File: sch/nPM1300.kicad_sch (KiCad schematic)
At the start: 24 parts, among them J1 USB_C_Receptacle_USB2.0_16P, J4 Conn_01x02_MountingPin, U2 nPM1300-QEAA, U5 USBLC6-2P6

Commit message: Updates for rev 1
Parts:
- added D2: LED_Red, LED_SMD:LED_0603_1608Metric, symbol Device:LED_Small
- added D3: LED_Green, LED_SMD:LED_0603_1608Metric, symbol Device:LED_Small
- added D4: LED_Blue, LED_SMD:LED_0603_1608Metric, symbol Device:LED_Small
- added TP10, TP11, TP12, TP13, TP3, TP4, TP5, TP6, TP7, TP8, TP9: TestPoint, TestPoint:TestPoint_Pad_D1.0mm, symbol Connector:TestPoint
- C14, C21: LCSC (none) -> C15849
- C15: LCSC (none) -> C467016
- C16, C17, C18, C19, C22, C23, C24, C25, C26: LCSC (none) -> C19702
- C20: LCSC (none) -> C23630
- F1: LCSC (none) -> C516069
- J1: LCSC (none) -> C165948
- J4: LCSC (none) -> C5118738
- L5, L6: LCSC (none) -> C412023
- R2: LCSC (none) -> C138139
- R3: LCSC (none) -> C274343
- R6, R7: LCSC (none) -> C270344
- U2: LCSC (none) -> C7466043
- U5: LCSC (none) -> C15999
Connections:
- net NTC is gone; now on net GND: U2.18 (NTC)
- net LSOUT1: now also TP9.1
- net LSOUT2: now also TP10.1
- net SCL: now also TP12.1
- net SDA: now also TP11.1
- net VBUSIN: now also TP4.1
- net VBUSOUT: now also TP6.1
- net VDD_SX1262: now also TP8.1
- net VDD_nRF: now also TP7.1
- net nPM1300.INT: now also TP13.1
- net VSYS: now reaches C16.1, C17.1, C18.1, U2.20 (VSYS), U2.4 (PVDD)
- net VSYS: now also D2.2 (A), D3.2 (A), D4.2 (A), TP5.1
- net at C20.1, J4.1 (Pin_1), U2.19 (VBAT): now also TP3.1
- net LED0: now reaches U2.25 (LED0)
- net LED0: now also D2.1 (K)
- net LED1: now reaches U2.26 (LED1)
- net LED1: now also D3.1 (K)
- net LED2: now reaches U2.27 (LED2)
- net LED2: now also D4.1 (K)
- no-connect marks 9 -> 6

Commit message: Updates
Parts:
- J1: footprint amemb-Connector_USB:USB_C_Receptacle_HRO_TYPE-C-31-M-12-Edge_Silkscreen_Removed -> easyeda2kicad:USB_C_Receptacle_HRO_TYPE-C-31-M-12-Edge_Silkscreen_Removed
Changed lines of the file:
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@@
 			)
 		)
-		(property "Footprint" "amemb-Connector_USB:USB_C_Receptacle_HRO_TYPE-C-31-M-12-Edge_Silkscreen_Removed"
+		(property "Footprint" "easyeda2kicad:USB_C_Receptacle_HRO_TYPE-C-31-M-12-Edge_Silkscreen_Removed"
 			(at 59.69 88.9 0)
 			(hide yes)
@@
 	)
 	(group "USB-C Receptacle with ESD + 1A fuse"
-		(lib_id "amemb-USB:USB-C Receptacle with ESD + 1A fuse")
+		(lib_id "Sidewalk_Devkit:USB-C Receptacle with ESD + 1A fuse")
 		(members "0bc2f94f-7181-411a-8b65-34718c7d9534" "0d027d96-20b3-4857-adf6-a3024518c9e7"
 			"1803beea-17d5-4564-9914-ef8df8ad989e" "212863e6-77aa-411a-9ec4-98ee8b9264cc"

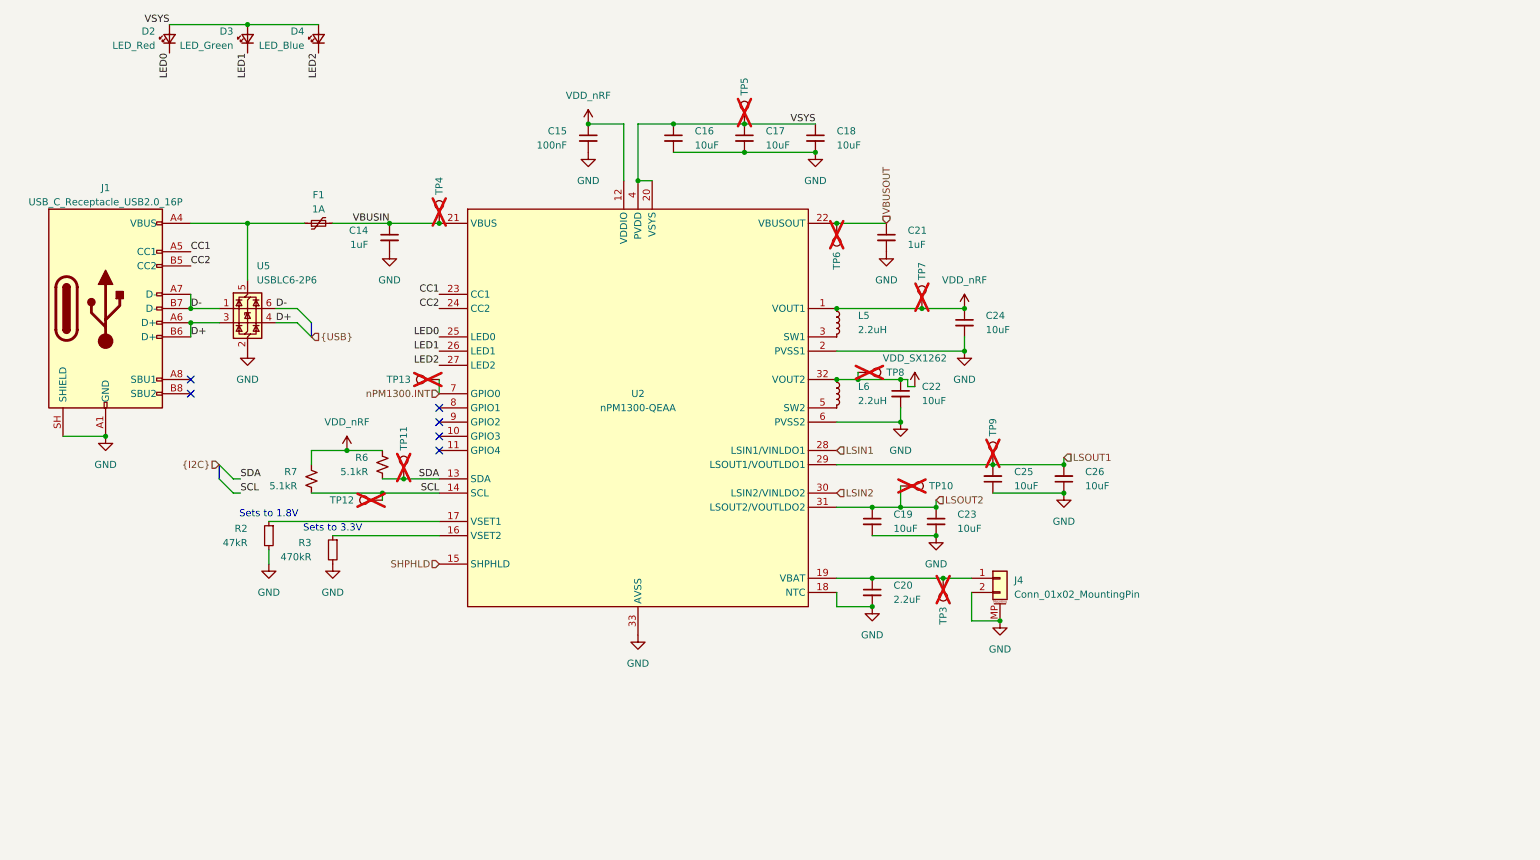
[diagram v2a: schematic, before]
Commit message: Added external current measurement for L15 and SX1262
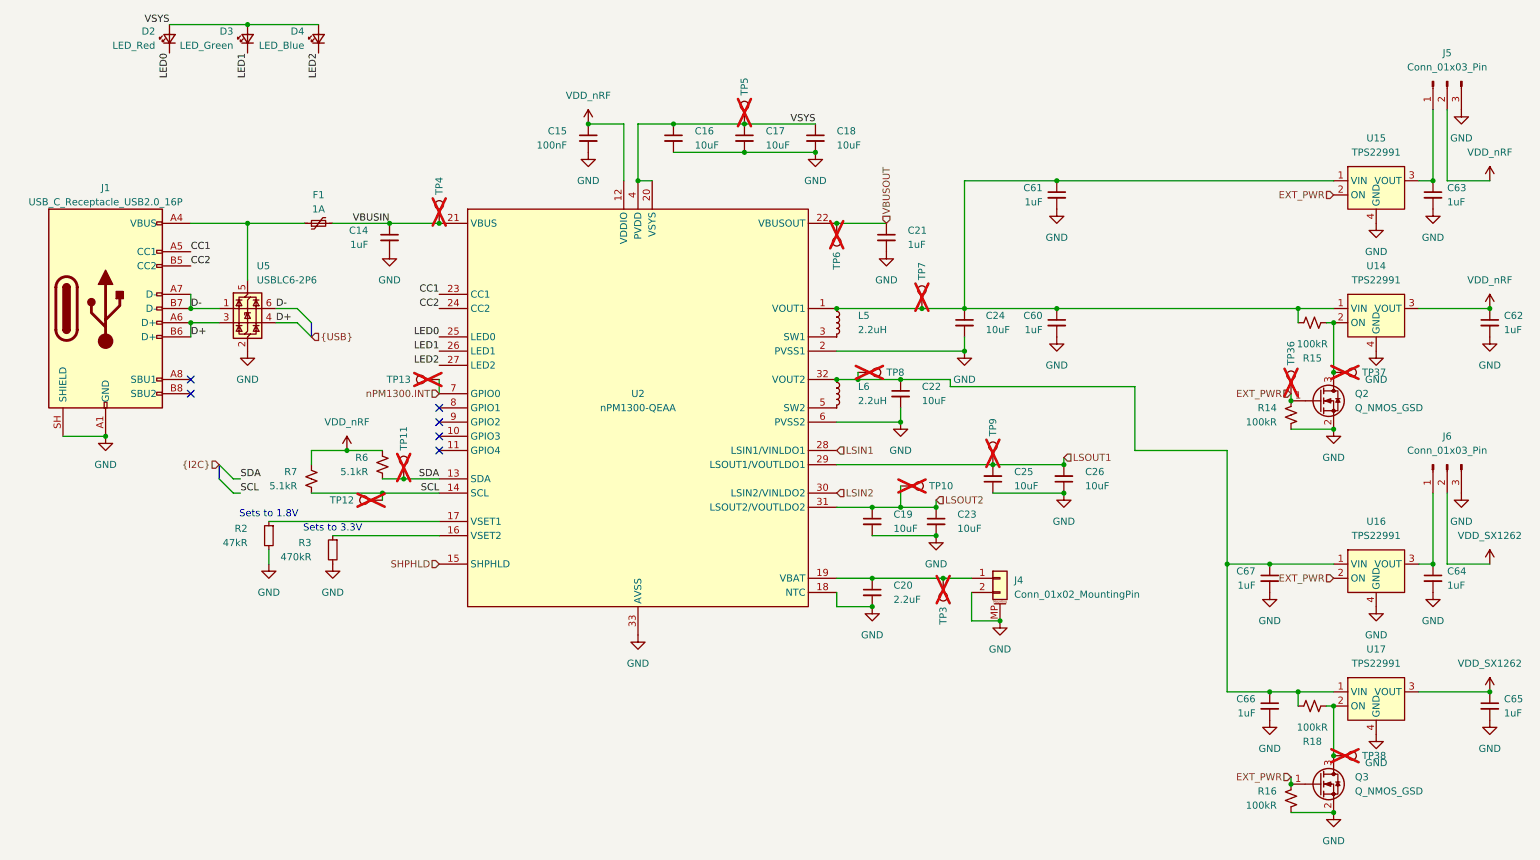
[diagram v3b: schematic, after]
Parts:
- added C60, C61, C62, C63, C64, C65, C66, C67: 1uF, passives:C_0201_0603Metric_L, symbol Device:C_Small
- added J5, J6: Conn_01x03_Pin, Connector_PinHeader_2.54mm:PinHeader_1x03_P2.54mm_Vertical, symbol Connector:Conn_01x03_Pin
- added Q2, Q3: Q_NMOS_GSD, Package_DFN_QFN:Diodes_DFN1006-3, symbol Transistor_FET:Q_NMOS_GSD
- added R14, R15, R16, R18: 100kR, passives:C_0201_0603Metric_L, symbol Device:R_Small_US
- added TP36, TP37, TP38: TestPoint, TestPoint:TestPoint_Pad_D1.0mm, symbol Connector:TestPoint
- added U14, U15, U16, U17: TPS22991, easyeda2kicad:4-UQFN-0.9x0.8mm, symbol easyeda2kicad:TPS22991
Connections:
- net GND: now also C60.2, C61.2, C62.2, C63.2, C64.2, C65.2, C66.2, C67.2, J5.3 (Pin_3), J6.3 (Pin_3), Q2.2 (S), Q3.2 (S), R14.2, R16.2, U14.4 (GND), U15.4 (GND), U16.4 (GND), U17.4 (GND)
- net VDD_SX1262: now also C65.1, J6.2 (Pin_2), U17.3 (VOUT); no longer C22.1, L6.2, TP8.1, U2.32 (VOUT2)
- net VDD_nRF: now also C62.1, J5.2 (Pin_2), U14.3 (VOUT); no longer C24.1, L5.1, TP7.1, U2.1 (VOUT1)
- new net: Q2.3 (D), R15.2, TP37.1, U14.2 (ON)
- new net: C22.1, C66.1, C67.1, L6.2, R18.1, TP8.1, U16.1 (VIN), U17.1 (VIN), U2.32 (VOUT2)
- new net: C64.1, J6.1 (Pin_1), U16.3 (VOUT)
- new net: Q3.3 (D), R18.2, TP38.1, U17.2 (ON)
- new net: C63.1, J5.1 (Pin_1), U15.3 (VOUT)
- new net: C24.1, C60.1, C61.1, L5.1, R15.1, TP7.1, U14.1 (VIN), U15.1 (VIN), U2.1 (VOUT1)
- new net EXT_PWR: Q2.1 (G), Q3.1 (G), R14.1, R16.1, TP36.1, U15.2 (ON), U16.2 (ON)
